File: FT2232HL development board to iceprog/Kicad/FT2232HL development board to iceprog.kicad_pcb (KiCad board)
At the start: 2 copper layers, 37.6 x 51.3 mm, 4 parts, among them J1 Conn_02x05_Odd_Even, P1 Conn_01x19_Male, P2 Conn_01x19_Male

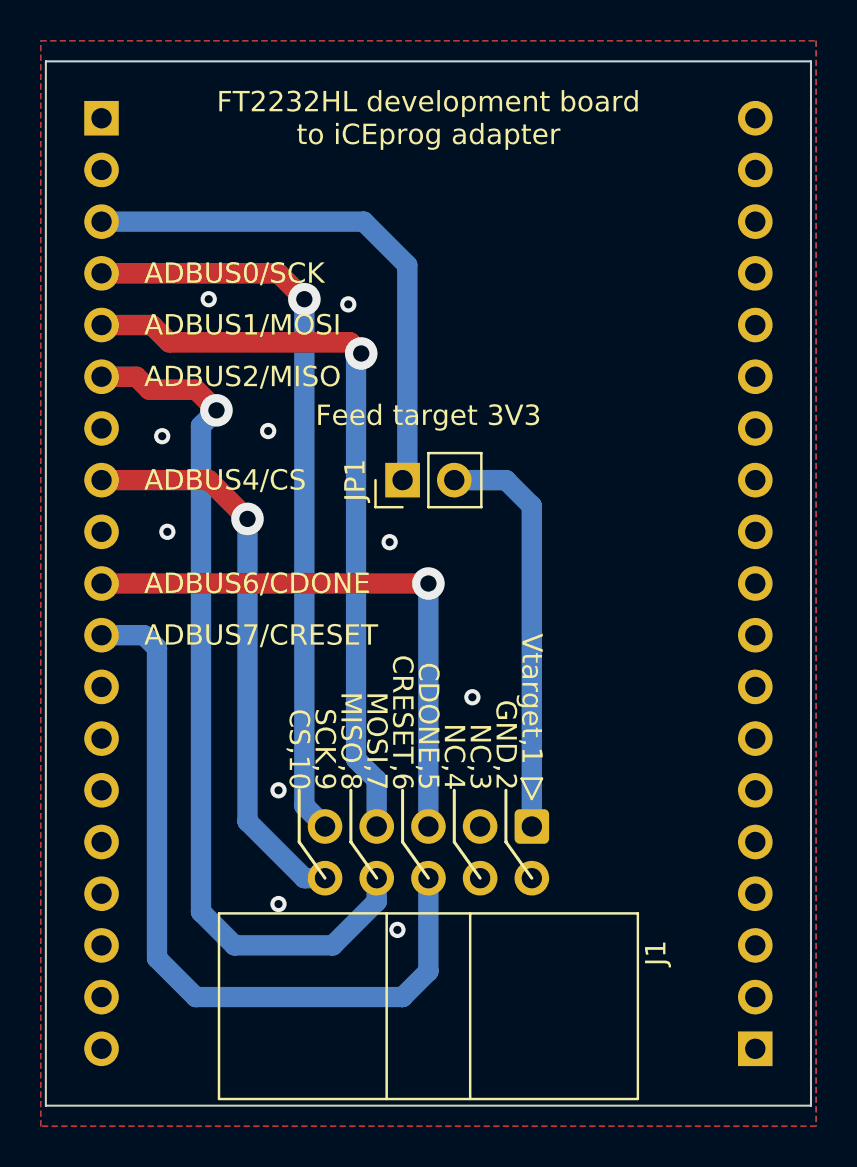
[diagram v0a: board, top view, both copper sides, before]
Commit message: Swapped MOSI/MISO.
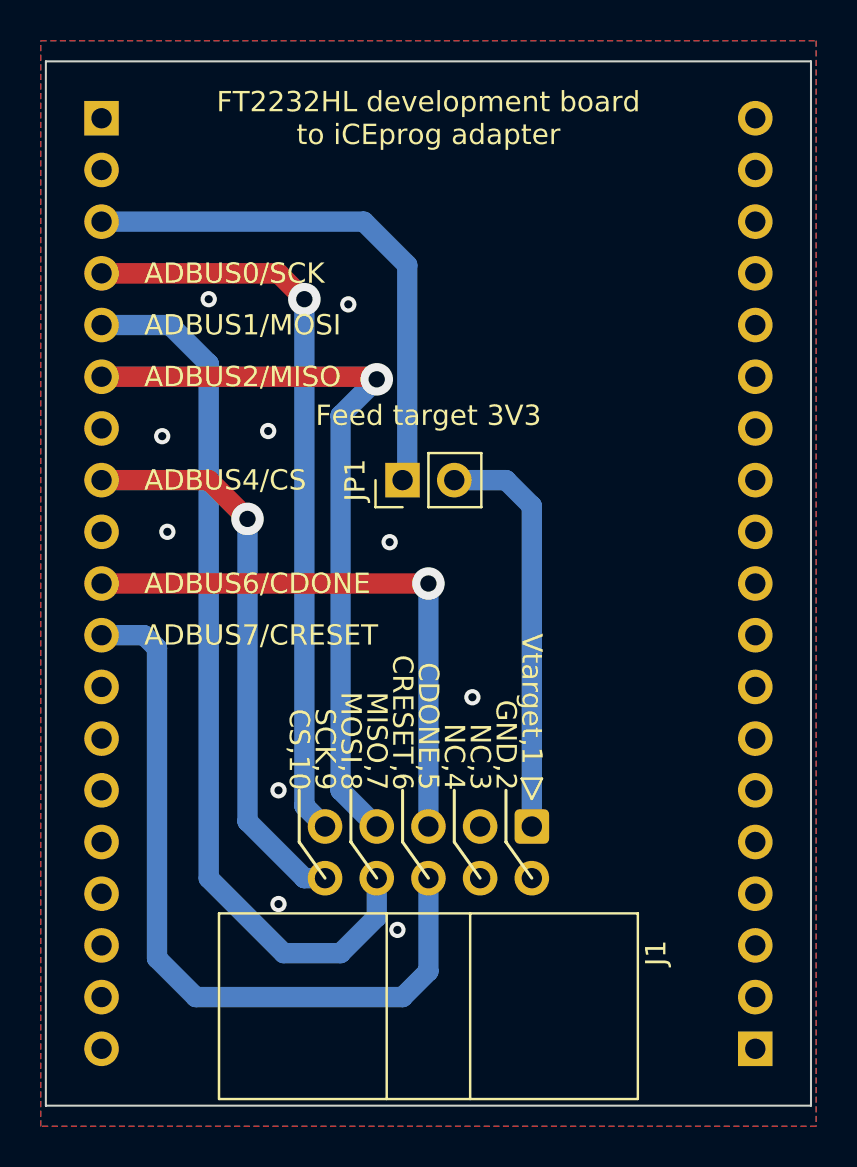
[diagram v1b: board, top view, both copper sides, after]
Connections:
- J1 pad 7: ADBUS1/MOSI -> ADBUS2/MISO
- J1 pad 8: ADBUS2/MISO -> ADBUS1/MOSI
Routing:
- net ADBUS1/MOSI: track 37.1 -> 43.7 mm, vias 1 -> 0
- net ADBUS2/MISO: track 42.6 -> 37.0 mm
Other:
- board text added: "2022-12-20 R1 https://github.com/atoomnetmarc /FT2232HL-development-board-adapters Apache License, version 2.0"
- board text added: "MISO,7"
- board text added: "MOSI,8"
- board text removed: "2022-12-20 https://github.com/atoomnetmarc /FT2232HL-development-board-adapters Apache License, version 2.0"
- board text removed: "MISO,8"
- board text removed: "MOSI,7"
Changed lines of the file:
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@@
   )
   (paper "A4")
+  (title_block
+    (title "FT2232HL development board to iceprog")
+    (date "2022-12-20")
+    (rev "1")
+    (company "https://github.com/atoomnetmarc/FT2232HL-development-board-adapters")
+  )
   (layers
     (0 "F.Cu" signal)
@@
       (net 8 "ADBUS7{slash}CRESET") (pinfunction "Pin_6") (pintype "passive"))
     (pad "7" thru_hole circle (at 0 7.62 270) (size 1.7 1.7) (drill 1) (layers *.Cu *.Mask)
-      (net 4 "ADBUS1{slash}MOSI") (pinfunction "Pin_7") (pintype "passive"))
+      (net 5 "ADBUS2{slash}MISO") (pinfunction "Pin_7") (pintype "passive"))
     (pad "8" thru_hole circle (at 2.54 7.62 270) (size 1.7 1.7) (drill 1) (layers *.Cu *.Mask)
-      (net 5 "ADBUS2{slash}MISO") (pinfunction "Pin_8") (pintype "passive"))
+      (net 4 "ADBUS1{slash}MOSI") (pinfunction "Pin_8") (pintype "passive"))
     (pad "9" thru_hole circle (at 0 10.16 270) (size 1.7 1.7) (drill 1) (layers *.Cu *.Mask)
       (net 3 "ADBUS0{slash}SCK") (pinfunction "Pin_9") (pintype "passive"))
@@
   (gr_line (start 18.796 82.296) (end 18.796 133.604) (layer "Edge.Cuts") (width 0.1))
   (gr_line (start -18.796 133.604) (end -18.796 82.296) (layer "Edge.Cuts") (width 0.1))
-  (gr_text "2022-12-20\nhttps://github.com/atoomnetmarc\n/FT2232HL-development-board-adapters\nApache License, version 2.0" (at 10.16 101.6 270) (layer "B.SilkS")
+  (gr_text "2022-12-20 R1\nhttps://github.com/atoomnetmarc\n/FT2232HL-development-board-adapters\nApache License, version 2.0" (at 10.16 101.6 270) (layer "B.SilkS")
     (effects (font (size 1 1) (thickness 0.15)) (justify mirror))
   )
@@
     (effects (font (size 1 1) (thickness 0.15)) (justify right))
   )
-  (gr_text "MOSI,7" (at -2.54 118.11 270) (layer "F.SilkS")
-    (effects (font (size 1 1) (thickness 0.15)) (justify right))
-  )
-  (gr_text "MISO,8" (at -3.81 118.11 270) (layer "F.SilkS")
+  (gr_text "MISO,7" (at -2.54 118.11 270) (layer "F.SilkS")
+    (effects (font (size 1 1) (thickness 0.15)) (justify right))
+  )
+  (gr_text "MOSI,8" (at -3.81 118.11 270) (layer "F.SilkS")
     (effects (font (size 1 1) (thickness 0.15)) (justify right))
   )
@@
   (segment (start -5.08 119.888) (end -6.096 118.872) (width 1) (layer "B.Cu") (net 3))
   (segment (start -6.096 118.872) (end -6.096 93.98) (width 1) (layer "B.Cu") (net 3))
-  (segment (start -3.849 96.1) (end -3.302 96.647) (width 1) (layer "F.Cu") (net 4))
-  (segment (start -13.589 95.25) (end -12.739 96.1) (width 1) (layer "F.Cu") (net 4))
-  (segment (start -16.06 95.25) (end -13.589 95.25) (width 1) (layer "F.Cu") (net 4))
-  (segment (start -12.739 96.1) (end -3.849 96.1) (width 1) (layer "F.Cu") (net 4))
-  (via (at -3.302 96.647) (size 1.6) (drill 0.8) (layers "F.Cu" "B.Cu") (net 4))
-  (segment (start -2.54 119.888) (end -2.54 117.602) (width 1) (layer "B.Cu") (net 4))
-  (segment (start -3.556 116.586) (end -3.556 96.901) (width 1) (layer "B.Cu") (net 4))
-  (segment (start -3.556 96.901) (end -3.302 96.647) (width 1) (layer "B.Cu") (net 4))
-  (segment (start -2.54 117.602) (end -3.556 116.586) (width 1) (layer "B.Cu") (net 4))
-  (segment (start -14.351 97.79) (end -13.716 98.425) (width 1) (layer "F.Cu") (net 5))
-  (segment (start -13.716 98.425) (end -11.43 98.425) (width 1) (layer "F.Cu") (net 5))
-  (segment (start -11.43 98.425) (end -10.414001 99.440999) (width 1) (layer "F.Cu") (net 5))
-  (segment (start -16.06 97.79) (end -14.351 97.79) (width 1) (layer "F.Cu") (net 5))
-  (via (at -10.414001 99.440999) (size 1.6) (drill 0.8) (layers "F.Cu" "B.Cu") (net 5))
-  (segment (start -11.176 100.202998) (end -10.414001 99.440999) (width 1) (layer "B.Cu") (net 5))
-  (segment (start -4.699 125.73) (end -9.525 125.73) (width 1) (layer "B.Cu") (net 5))
-  (segment (start -11.176 124.079) (end -11.176 100.202998) (width 1) (layer "B.Cu") (net 5))
-  (segment (start -9.525 125.73) (end -11.176 124.079) (width 1) (layer "B.Cu") (net 5))
-  (segment (start -2.54 122.428) (end -2.54 123.571) (width 1) (layer "B.Cu") (net 5))
-  (segment (start -2.54 123.571) (end -4.699 125.73) (width 1) (layer "B.Cu") (net 5))
+  (segment (start -2.54 124.333) (end -2.54 122.428) (width 1) (layer "B.Cu") (net 4))
+  (segment (start -7.112 126.111) (end -4.318 126.111) (width 1) (layer "B.Cu") (net 4))
+  (segment (start -16.06 95.25) (end -12.7 95.25) (width 1) (layer "B.Cu") (net 4))
+  (segment (start -10.795 122.428) (end -7.112 126.111) (width 1) (layer "B.Cu") (net 4))
+  (segment (start -4.318 126.111) (end -2.54 124.333) (width 1) (layer "B.Cu") (net 4))
+  (segment (start -10.795 97.155) (end -10.795 122.428) (width 1) (layer "B.Cu") (net 4))
+  (segment (start -12.7 95.25) (end -10.795 97.155) (width 1) (layer "B.Cu") (net 4))
+  (segment (start -16.06 97.79) (end -2.667 97.79) (width 1) (layer "F.Cu") (net 5))
+  (segment (start -2.667 97.79) (end -2.54 97.917) (width 1) (layer "F.Cu") (net 5))
+  (via (at -2.54 97.917) (size 1.6) (drill 0.8) (layers "F.Cu" "B.Cu") (net 5))
+  (segment (start -2.54 119.888) (end -4.318 118.11) (width 1) (layer "B.Cu") (net 5))
+  (segment (start -4.318 118.11) (end -4.318 99.695) (width 1) (layer "B.Cu") (net 5))
+  (segment (start -4.318 99.695) (end -2.54 97.917) (width 1) (layer "B.Cu") (net 5))
   (segment (start -10.795 102.87) (end -8.89 104.775) (width 1) (layer "F.Cu") (net 6))
   (segment (start -16.06 102.87) (end -10.795 102.87) (width 1) (layer "F.Cu") (net 6))
